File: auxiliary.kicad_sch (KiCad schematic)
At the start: 3 parts, among them J7 Conn_01x05

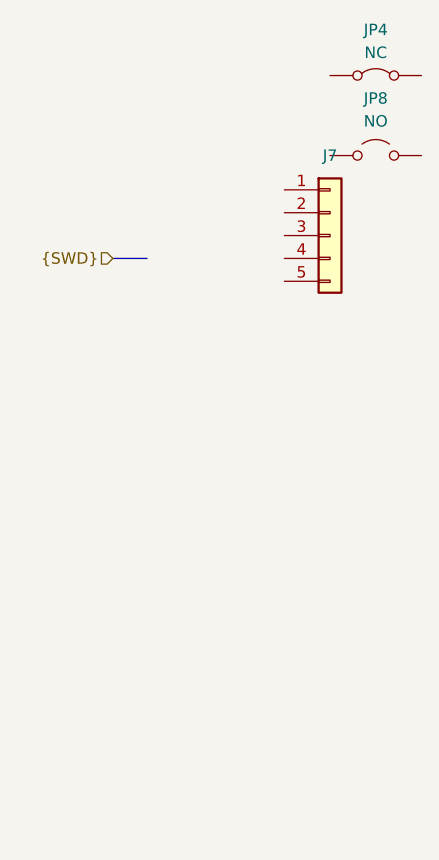
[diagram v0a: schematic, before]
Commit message: added auxialry - swd connector and NRST pin circuit
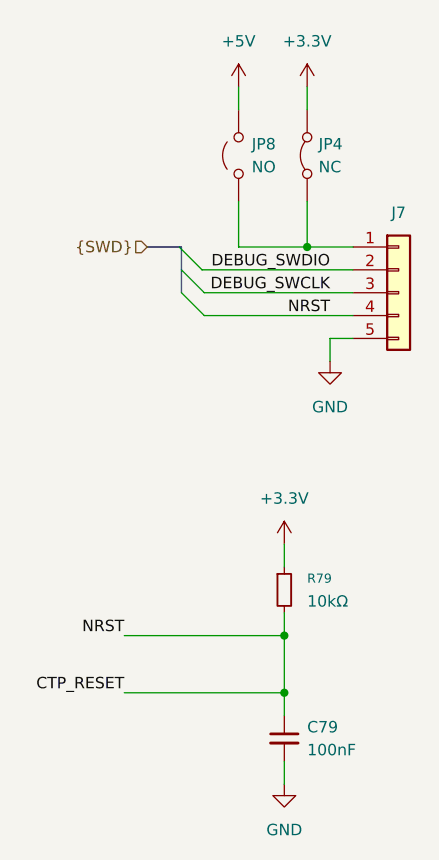
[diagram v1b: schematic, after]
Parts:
- added C79: 100nF, 0_capacitors:C_0402_1005Metric, symbol 0_capacitors:CL05B104KO5NNNC
- added R79: 10kΩ, 0_resistors:R_0402_1005Metric, symbol 0_resistors:0402WGF1002TCE
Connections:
- net at J7.1 (Pin_1): now also JP4.1 (A), JP8.2 (B)
- net DEBUG_SWDIO: now reaches J7.2 (Pin_2)
- net DEBUG_SWCLK: now reaches J7.3 (Pin_3)
- net CTP_RESET: now reaches J7.4 (Pin_4)
- net CTP_RESET: now also C79.1, R79.2
- net GND: now reaches J7.5 (Pin_5)
- net GND: now also C79.2
- net +5V: now reaches JP8.1 (A)
- net +3.3V: now reaches JP4.2 (B)
- net +3.3V: now also R79.1
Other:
- moved on the sheet: J7, JP4, JP8

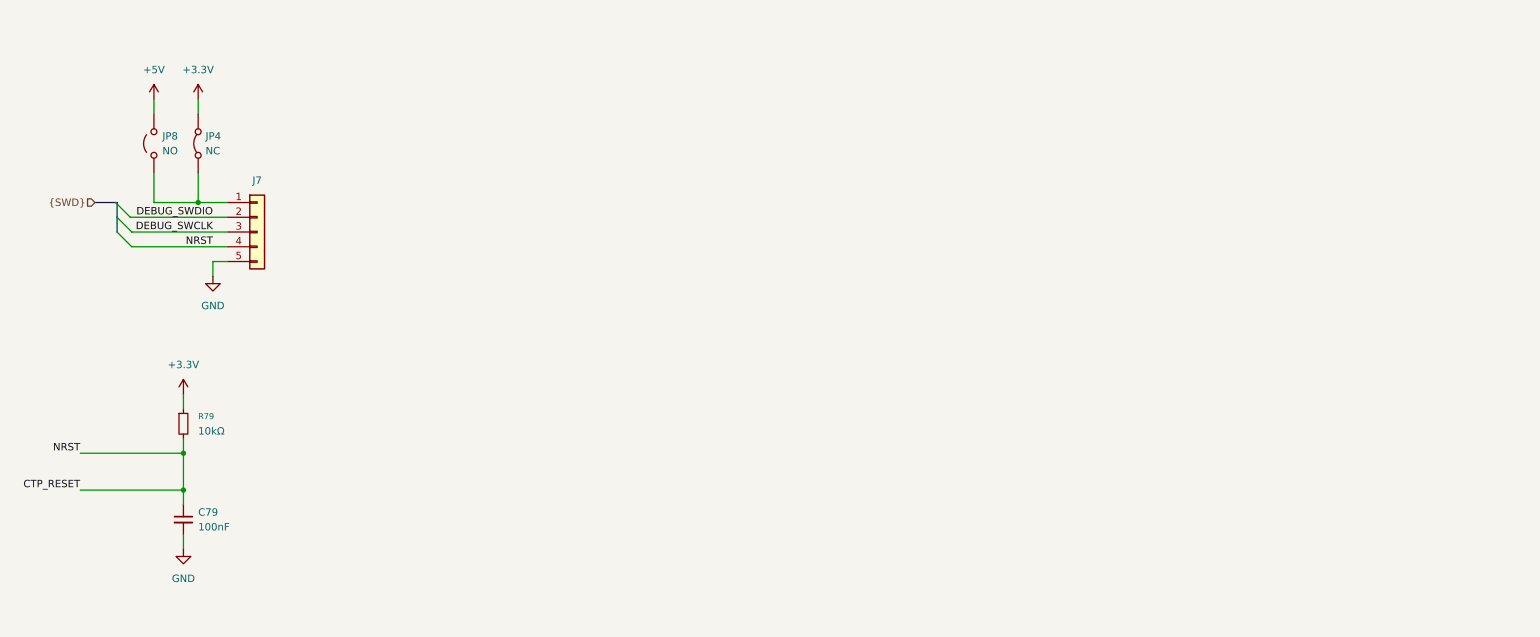
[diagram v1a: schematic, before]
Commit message: added schematic for crystal oscillators
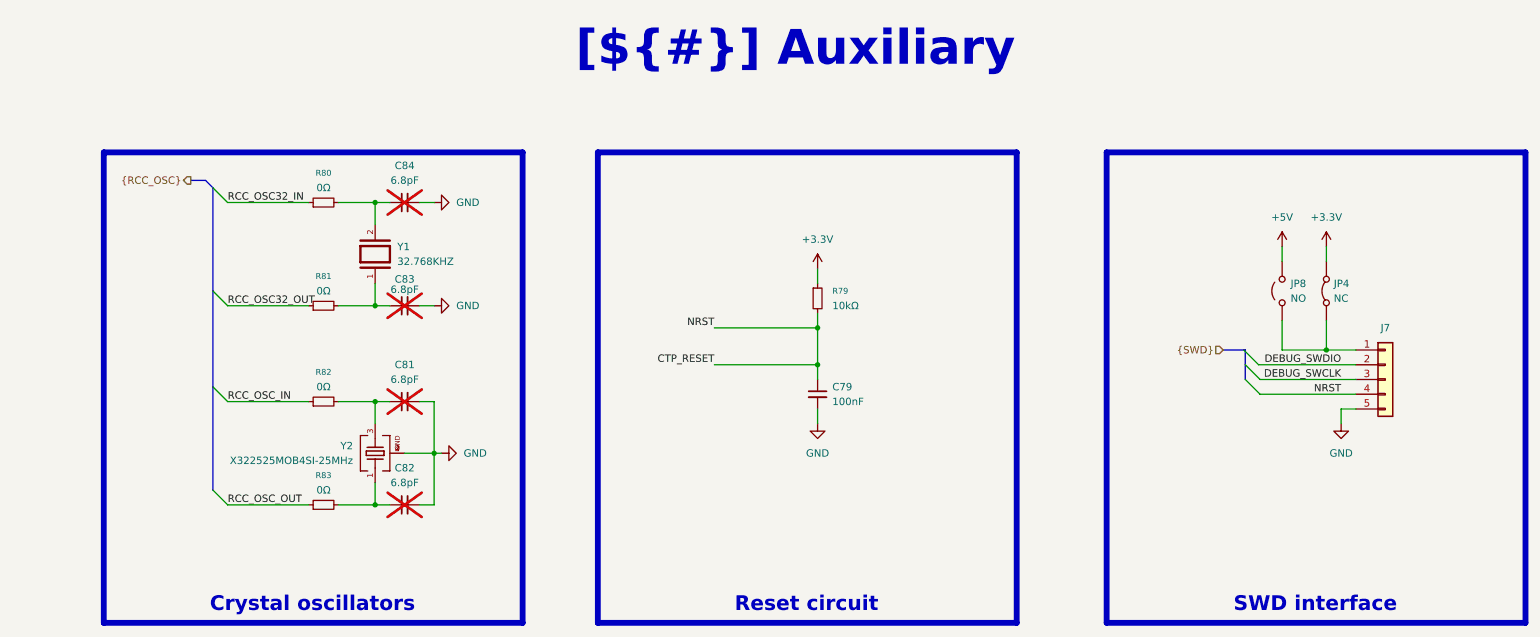
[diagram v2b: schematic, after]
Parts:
- added C81, C82, C83, C84: 6.8pF, 0_capacitors:C_0402_1005Metric, symbol 0_capacitors:0402CG6R8C500NT
- added R80, R81, R82, R83: 0Ω, 0_resistors:R_0402_1005Metric, symbol 0_resistors:0402WGF0000TCE
- added Y1: 32.768KHZ, 0_oscillators:X322525MOB4SI 25MHz, symbol 0_oscillators:Q13FC13500004-32.768KHZ-4-T
- added Y2: X322525MOB4SI-25MHz, 0_oscillators:X322525MOB4SI 25MHz, symbol 0_oscillators:X322525MOB4SI
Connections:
- net GND: now also C81.2, C82.2, C83.2, C84.2, Y2.2, Y2.4
- new net: C82.1, R83.2, Y2.1
- new net: C81.1, R82.2, Y2.3
- new net: C83.1, R81.2, Y1.1
- new net: C84.1, R80.2, Y1.2
- new net RCC_OSC32_IN: R80.1
- new net RCC_OSC32_OUT: R81.1
- new net RCC_OSC_IN: R82.1
- new net RCC_OSC_OUT: R83.1
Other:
- title: (none) -> Auxiliary
- moved on the sheet: C79, J7, JP4, JP8, R79
